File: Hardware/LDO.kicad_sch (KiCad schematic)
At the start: 5 parts, among them U3 MCP1826S

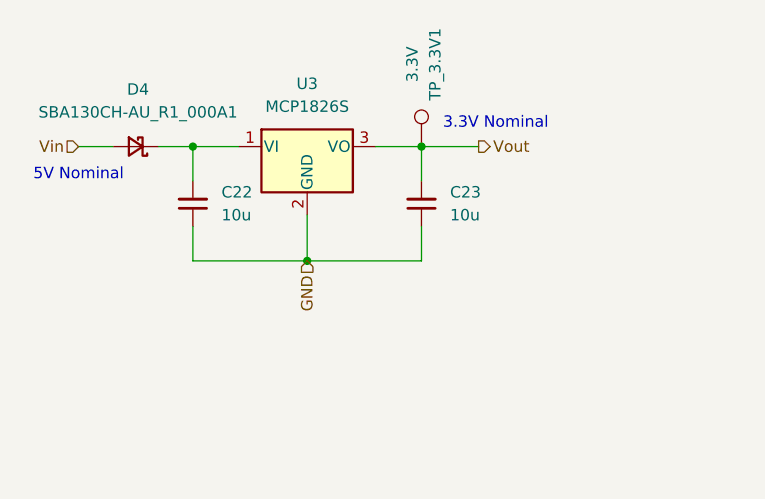
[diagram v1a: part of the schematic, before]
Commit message: Added TestPoints
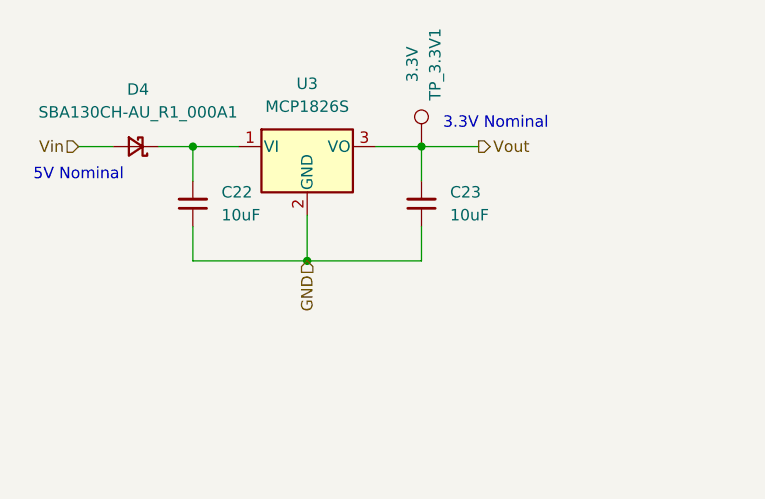
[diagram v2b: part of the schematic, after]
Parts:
- C22, C23: value 10u -> 10uF; footprint Capacitor_SMD:C_0805_2012Metric_Pad1.18x1.45mm_HandSolder -> Capacitor_SMD:C_0603_1608Metric_Pad1.08x0.95mm_HandSolder
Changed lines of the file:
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@@
 			)
 		)
-		(property "Value" "10u"
+		(property "Value" "10uF"
 			(at 168.275 71.1135 0)
 			(show_name no)
@@
 			)
 		)
-		(property "Footprint" "Capacitor_SMD:C_0805_2012Metric_Pad1.18x1.45mm_HandSolder"
+		(property "Footprint" "Capacitor_SMD:C_0603_1608Metric_Pad1.08x0.95mm_HandSolder"
 			(at 165.1 69.85 0)
 			(hide yes)
@@
 			)
 		)
-		(property "Value" "10u"
+		(property "Value" "10uF"
 			(at 142.875 71.1135 0)
 			(show_name no)
@@
 			)
 		)
-		(property "Footprint" "Capacitor_SMD:C_0805_2012Metric_Pad1.18x1.45mm_HandSolder"
+		(property "Footprint" "Capacitor_SMD:C_0603_1608Metric_Pad1.08x0.95mm_HandSolder"
 			(at 139.7 69.85 0)
 			(hide yes)

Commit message: Made some changes
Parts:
- removed TP_3.3V1: 3.3V, TestPoint:TestPoint_Loop_D1.80mm_Drill1.0mm_Beaded, symbol Connector:TestPoint
- C22, C23: value 10uF -> 10u; footprint Capacitor_SMD:C_0603_1608Metric_Pad1.08x0.95mm_HandSolder -> Capacitor_SMD:C_0805_2012Metric_Pad1.18x1.45mm_HandSolder
- U3: LCSC MFG P/N LM39100S-3.3 -> (none)
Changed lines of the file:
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@@
 			)
 		)
-		(property "Value" "10uF"
+		(property "Value" "10u"
 			(at 168.275 71.1135 0)
 			(show_name no)
@@
 			)
 		)
-		(property "Footprint" "Capacitor_SMD:C_0603_1608Metric_Pad1.08x0.95mm_HandSolder"
+		(property "Footprint" "Capacitor_SMD:C_0805_2012Metric_Pad1.18x1.45mm_HandSolder"
 			(at 165.1 69.85 0)
 			(hide yes)
@@
 		)
 		(instances
-			(project "power_Rail"
-				(path "/aa7870c6-fc66-461c-9d29-908d06b1b5db/7da03bba-6e89-4676-b538-830a2c925006"
+			(project "LDO"
+				(path "/8ff43370-8d10-4d2c-b1a3-81d1c2934a98"
+					(reference "C2")
+					(unit 1)
+				)
+			)
+			(project "LeaderSOMBreakout"
+				(path "/e5b32072-3e3d-42a6-9d41-1a76d538e329/f3053c74-1ac6-4a33-80f3-565e8c4c2c7d"
+					(reference "C?")
+					(unit 1)
+				)
+			)
+			(project "SuspensionBoard"
+				(path "/f9dc491a-b8c6-4623-9728-13837ac4bba3/bb9a0353-c4c7-4944-b892-c85c279a5c68/327f7d27-fafc-4ab2-b214-d55abcefb420"
 					(reference "C23")
-					(unit 1)
-				)
-			)
-			(project "SuspensionBoard"
-				(path "/f9dc491a-b8c6-4623-9728-13837ac4bba3/bb9a0353-c4c7-4944-b892-c85c279a5c68/7da03bba-6e89-4676-b538-830a2c925006"
-					(reference "C23")
-					(unit 1)
-				)
-			)
-		)
-	)
-	(symbol
-		(lib_id "Connector:TestPoint")
-		(at 165.1 63.5 0)
-		(unit 1)
-		(body_style 1)
-		(exclude_from_sim no)
-		(in_bom no)
-		(on_board yes)
-		(in_pos_files yes)
-		(dnp no)
-		(property "Reference" "TP_3.3V1"
-			(at 166.624 54.356 90)
-			(show_name no)
-			(do_not_autoplace no)
-			(effects
-				(font
-					(size 1.27 1.27)
-				)
-			)
-		)
-		(property "Value" "3.3V"
-			(at 164.084 54.356 90)
-			(show_name no)
-			(do_not_autoplace no)
-			(effects
-				(font
-					(size 1.27 1.27)
-				)
-			)
-		)
-		(property "Footprint" "TestPoint:TestPoint_Loop_D1.80mm_Drill1.0mm_Beaded"
-			(at 170.18 63.5 0)
-			(hide yes)
-			(show_name no)
-			(do_not_autoplace no)
-			(effects
-				(font
-					(size 1.27 1.27)
-				)
-			)
-		)
-		(property "Datasheet" ""
-			(at 170.18 63.5 0)
-			(hide yes)
-			(show_name no)
-			(do_not_autoplace no)
-			(effects
-				(font
-					(size 1.27 1.27)
-				)
-			)
-		)
-		(property "Description" "test point"
-			(at 165.1 63.5 0)
-			(hide yes)
-			(show_name no)
-			(do_not_autoplace no)
-			(effects
-				(font
-					(size 1.27 1.27)
-				)
-			)
-		)
-		(property "Color" ""
-			(at 165.1 63.5 0)
-			(show_name no)
-			(do_not_autoplace no)
-			(effects
-				(font
-					(size 1.27 1.27)
-				)
-			)
-		)
-		(property "If" ""
-			(at 165.1 63.5 0)
-			(show_name no)
-			(do_not_autoplace no)
-			(effects
-				(font
-					(size 1.27 1.27)
-				)
-			)
-		)
-		(property "Mfg" ""
-			(at 165.1 63.5 0)
-			(show_name no)
-			(do_not_autoplace no)
-			(effects
-				(font
-					(size 1.27 1.27)
-				)
-			)
-		)
-		(property "Vf" ""
-			(at 165.1 63.5 0)
-			(show_name no)
-			(do_not_autoplace no)
-			(effects
-				(font
-					(size 1.27 1.27)
-				)
-			)
-		)
-		(pin "1"
-		)
-		(instances
-			(project "power_Rail"
-				(path "/aa7870c6-fc66-461c-9d29-908d06b1b5db/7da03bba-6e89-4676-b538-830a2c925006"
-					(reference "TP_3.3V1")
-					(unit 1)
-				)
-			)
-			(project "SuspensionBoard"
-				(path "/f9dc491a-b8c6-4623-9728-13837ac4bba3/bb9a0353-c4c7-4944-b892-c85c279a5c68/7da03bba-6e89-4676-b538-830a2c925006"
-					(reference "TP_3.3V1")
 					(unit 1)
 				)
@@
 			)
 		)
-		(property "LCSC MFG P/N" "LM39100S-3.3"
-			(at 152.4 63.5 0)
-			(hide yes)
-			(show_name no)
-			(do_not_autoplace no)
-			(effects
-				(font
-					(size 1.27 1.27)
-				)
-			)
-		)
 		(pin "2"
 		)
@@
 		)
 		(instances
-			(project "power_Rail"
-				(path "/aa7870c6-fc66-461c-9d29-908d06b1b5db/7da03bba-6e89-4676-b538-830a2c925006"
-					(reference "U3")
+			(project "LDO"
+				(path "/8ff43370-8d10-4d2c-b1a3-81d1c2934a98"
+					(reference "U1")
 					(unit 1)
 				)
 			)
 			(project "SuspensionBoard"
-				(path "/f9dc491a-b8c6-4623-9728-13837ac4bba3/bb9a0353-c4c7-4944-b892-c85c279a5c68/7da03bba-6e89-4676-b538-830a2c925006"
+				(path "/f9dc491a-b8c6-4623-9728-13837ac4bba3/bb9a0353-c4c7-4944-b892-c85c279a5c68/327f7d27-fafc-4ab2-b214-d55abcefb420"
 					(reference "U3")
 					(unit 1)
@@
 		)
 		(instances
-			(project "power_Rail"
-				(path "/aa7870c6-fc66-461c-9d29-908d06b1b5db/7da03bba-6e89-4676-b538-830a2c925006"
-					(reference "D4")
+			(project "LDO"
+				(path "/8ff43370-8d10-4d2c-b1a3-81d1c2934a98"
+					(reference "D1")
 					(unit 1)
 				)
 			)
 			(project "SuspensionBoard"
-				(path "/f9dc491a-b8c6-4623-9728-13837ac4bba3/bb9a0353-c4c7-4944-b892-c85c279a5c68/7da03bba-6e89-4676-b538-830a2c925006"
+				(path "/f9dc491a-b8c6-4623-9728-13837ac4bba3/bb9a0353-c4c7-4944-b892-c85c279a5c68/327f7d27-fafc-4ab2-b214-d55abcefb420"
 					(reference "D4")
 					(unit 1)
@@
 			)
 		)
-		(property "Value" "10uF"
+		(property "Value" "10u"
 			(at 142.875 71.1135 0)
 			(show_name no)
@@
 			)
 		)
-		(property "Footprint" "Capacitor_SMD:C_0603_1608Metric_Pad1.08x0.95mm_HandSolder"
+		(property "Footprint" "Capacitor_SMD:C_0805_2012Metric_Pad1.18x1.45mm_HandSolder"
 			(at 139.7 69.85 0)
 			(hide yes)
@@
 		)
 		(instances
-			(project "power_Rail"
-				(path "/aa7870c6-fc66-461c-9d29-908d06b1b5db/7da03bba-6e89-4676-b538-830a2c925006"
+			(project "LDO"
+				(path "/8ff43370-8d10-4d2c-b1a3-81d1c2934a98"
+					(reference "C1")
+					(unit 1)
+				)
+			)
+			(project ""
+				(path "/e5b32072-3e3d-42a6-9d41-1a76d538e329/f3053c74-1ac6-4a33-80f3-565e8c4c2c7d"
+					(reference "C?")
+					(unit 1)
+				)
+			)
+			(project "SuspensionBoard"
+				(path "/f9dc491a-b8c6-4623-9728-13837ac4bba3/bb9a0353-c4c7-4944-b892-c85c279a5c68/327f7d27-fafc-4ab2-b214-d55abcefb420"
 					(reference "C22")
 					(unit 1)
-				)
-			)
-			(project "SuspensionBoard"
-				(path "/f9dc491a-b8c6-4623-9728-13837ac4bba3/bb9a0353-c4c7-4944-b892-c85c279a5c68/7da03bba-6e89-4676-b538-830a2c925006"
-					(reference "C22")
-					(unit 1)
